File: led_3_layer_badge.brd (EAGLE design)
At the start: 160 x 100 mm, 59 parts, among them U1 ATMEGA168, U2 MCP73811, U3 AP34063, U4 PCA9952

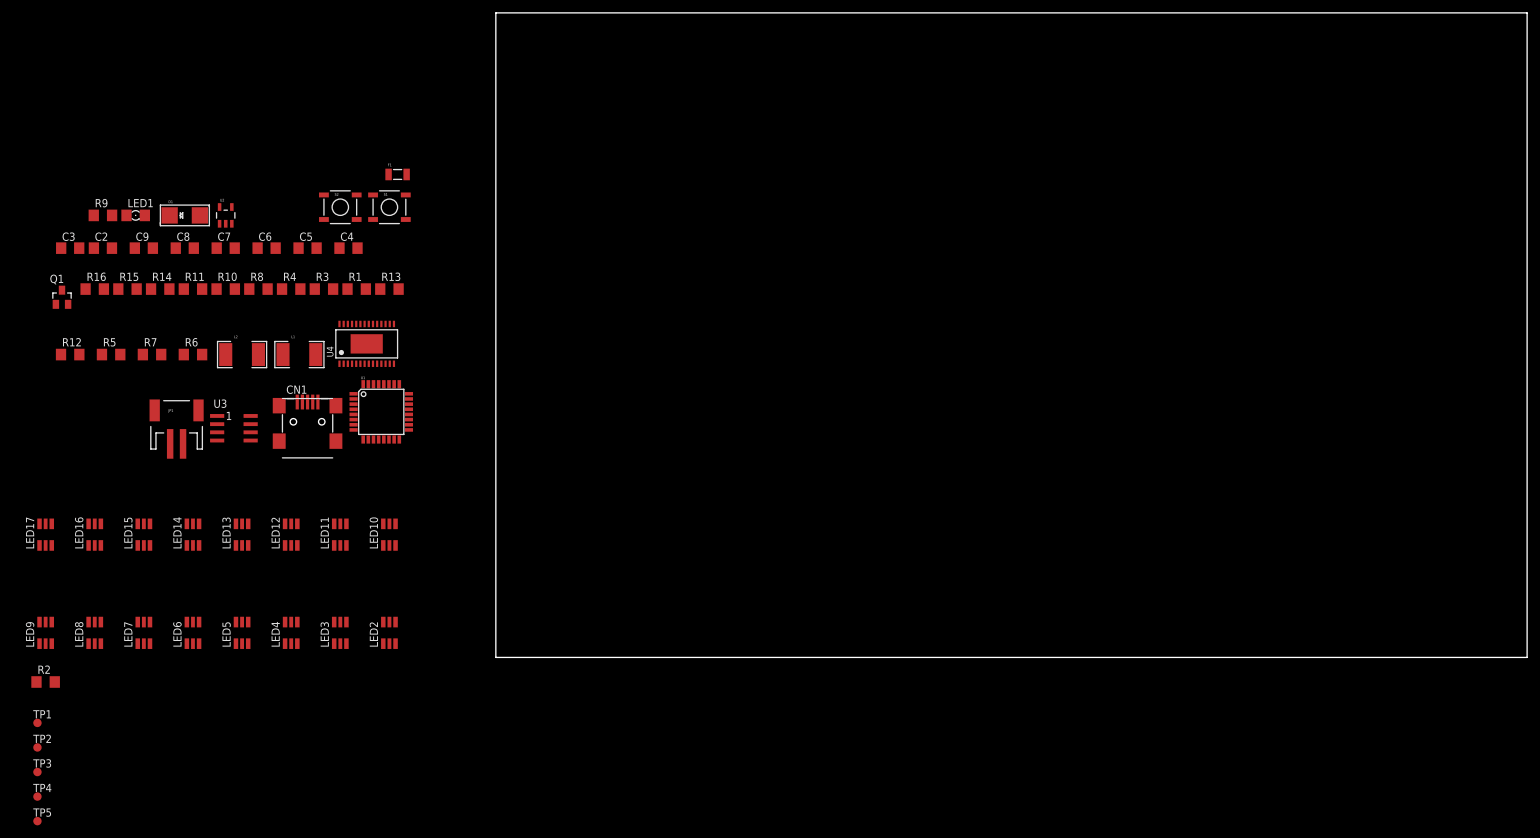
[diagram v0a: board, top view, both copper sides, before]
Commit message: added new concept image, found proper leds
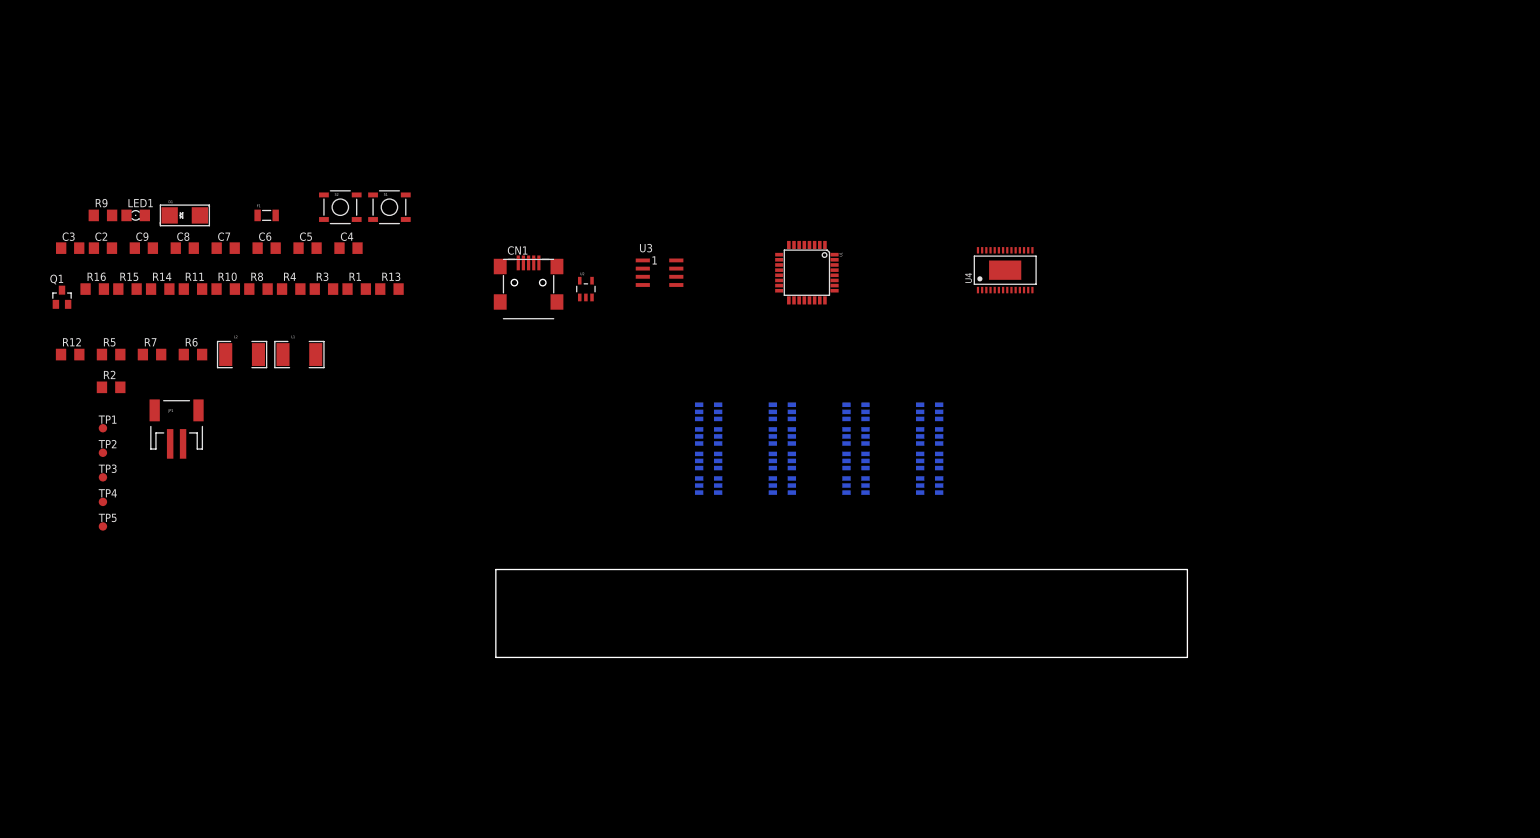
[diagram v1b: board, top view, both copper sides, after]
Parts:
- LED10, LED11, LED12, LED13, LED14, LED15, LED16, LED17, LED2, LED3, LED4, LED5, LED6, LED7, LED8, LED9: value GM5WA94310A -> GFTG-T7AW; device led:GM5WA94310A -> osram:C63062-A4-7-A1-01
- moved LED6 117.4 mm to (67.3, 30.5), flipped to the bottom, turned to 180 degrees
- moved LED14 115.9 mm to (67.3, 38.1), flipped to the bottom, turned to 180 degrees
- moved LED7 113.7 mm to (55.9, 30.5), flipped to the bottom, turned to 180 degrees
- moved LED15 112.1 mm to (55.9, 38.1), flipped to the bottom, turned to 180 degrees
- moved LED8 110.0 mm to (44.5, 30.5), flipped to the bottom, turned to 180 degrees
- moved LED16 108.4 mm to (44.5, 38.1), flipped to the bottom, turned to 180 degrees
- moved LED9 106.3 mm to (33.0, 30.5), flipped to the bottom, turned to 180 degrees
- moved LED17 104.6 mm to (33.0, 38.1), flipped to the bottom, turned to 180 degrees
- moved U4 99.7 mm to (78.7, 59.7)
- moved LED2 86.9 mm to (67.3, 26.7), flipped to the bottom, turned to 180 degrees
- moved LED10 85.2 mm to (67.3, 34.3), flipped to the bottom, turned to 180 degrees
- moved LED3 83.2 mm to (55.9, 26.7), flipped to the bottom, turned to 180 degrees
- moved LED11 81.4 mm to (55.9, 34.3), flipped to the bottom, turned to 180 degrees
- moved LED4 79.6 mm to (44.5, 26.7), flipped to the bottom, turned to 180 degrees
- moved LED12 77.7 mm to (44.5, 34.3), flipped to the bottom, turned to 180 degrees
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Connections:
- net A0: now also LED2.C3; no longer LED2.5
- net A1: now also LED2.C2; no longer LED2.4
- net A2: now also LED2.C1; no longer LED2.6
- net B0: now also LED10.C3; no longer LED10.5
- net B1: now also LED10.C2; no longer LED10.4
- net B2: now also LED10.C1; no longer LED10.6
- net C0: now also LED6.C3; no longer LED6.5
- net C1: now also LED6.C2; no longer LED6.4
- net C2: now also LED6.C1; no longer LED6.6
- net D0: now also LED14.C3; no longer LED14.5
- net D1: now also LED14.C2; no longer LED14.4
- net D2: now also LED14.C1; no longer LED14.6
- net N$10: now also LED17.A1, LED17.A2, LED17.A3; no longer LED17.1, LED17.2, LED17.3
- net N$12: now also LED6.A1, LED7.C1; no longer LED6.2, LED7.5
- net N$16: now also LED6.A2, LED7.C2; no longer LED6.3, LED7.4
- net N$17: now also LED6.A3, LED7.C3; no longer LED6.1, LED7.6
- net N$18: now also LED7.A1, LED8.C1; no longer LED8.2, LED9.5
- net N$19: now also LED7.A2, LED8.C2; no longer LED8.3, LED9.4
- net N$2: now also LED2.A1, LED3.C1; no longer LED2.2, LED3.5
- net N$20: now also LED7.A3, LED8.C3; no longer LED8.1, LED9.6
- net N$21: now also LED8.A1, LED9.C1; no longer LED7.2, LED8.5
- net N$22: now also LED8.A2, LED9.C2; no longer LED7.3, LED8.4
- net N$24: now also LED2.A2, LED3.C2; no longer LED2.3, LED3.4
- net N$25: now also LED2.A3, LED3.C3; no longer LED2.1, LED3.6
- net N$28: now also LED3.A1, LED4.C1; no longer LED4.2, LED5.5
- net N$29: now also LED3.A2, LED4.C2; no longer LED4.3, LED5.4
- net N$30: now also LED3.A3, LED4.C3; no longer LED4.1, LED5.6
- net N$31: now also LED4.A1, LED5.C1; no longer LED3.2, LED4.5
- net N$32: now also LED4.A2, LED5.C2; no longer LED3.3, LED4.4
- net N$33: now also LED4.A3, LED5.C3; no longer LED3.1, LED4.6
- net N$34: now also LED8.A3, LED9.C3; no longer LED7.1, LED8.6
- net N$35: now also LED10.A1, LED11.C1; no longer LED10.2, LED11.5
- net N$36: now also LED10.A2, LED11.C2; no longer LED10.3, LED11.4
- net N$37: now also LED10.A3, LED11.C3; no longer LED10.1, LED11.6
- net N$38: now also LED11.A1, LED12.C1; no longer LED12.2, LED13.5
- net N$39: now also LED11.A2, LED12.C2; no longer LED12.3, LED13.4
- net N$40: now also LED11.A3, LED12.C3; no longer LED12.1, LED13.6
- net N$41: now also LED12.A1, LED13.C1; no longer LED11.2, LED12.5
- net N$42: now also LED12.A2, LED13.C2; no longer LED11.3, LED12.4
- net N$43: now also LED12.A3, LED13.C3; no longer LED11.1, LED12.6
- net N$44: now also LED14.A1, LED15.C1; no longer LED14.2, LED15.5
- net N$45: now also LED14.A2, LED15.C2; no longer LED14.3, LED15.4
- net N$46: now also LED14.A3, LED15.C3; no longer LED14.1, LED15.6
- net N$47: now also LED15.A1, LED16.C1; no longer LED16.2, LED17.5
- net N$48: now also LED15.A2, LED16.C2; no longer LED16.3, LED17.4
- net N$49: now also LED15.A3, LED16.C3; no longer LED16.1, LED17.6
- net N$50: now also LED16.A1, LED17.C1; no longer LED15.2, LED16.5
- net N$51: now also LED16.A2, LED17.C2; no longer LED15.3, LED16.4
- net N$52: now also LED16.A3, LED17.C3; no longer LED15.1, LED16.6
- net VCC/2: now also LED13.A1, LED13.A2, LED13.A3, LED5.A1, LED5.A2, LED5.A3, LED9.A1, LED9.A2, LED9.A3; no longer LED13.1, LED13.2, LED13.3, LED5.1, LED5.2, LED5.3, LED9.1, LED9.2, LED9.3
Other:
- board size 160 x 100 mm -> 107.3 x 13.6 mm

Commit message: revisions
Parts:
- removed JP1: (no value), sparkfun:JST-2-SMD
- removed R11: 10k, rcl:R1206
- removed U1: ATMEGA168, sparkfun:TQFP32-08
- added IC1: TINY24/44/84, atmel:SOIC14
- added TP6, TP7: PTR1B2,54, testpad:B2,54
- Q1: value (none) -> P-CH
- U3: value AP34063 -> MC33063A
- moved R8 76.9 mm to (-66.0, -14.0)
- moved U4 55.1 mm to (92.7, 6.35)
- moved U3 54.6 mm to (24.1, 5.08)
- moved CN1 54.1 mm to (14.0, 3.81)
- moved U2 46.4 mm to (21.6, 11.4), turned to 270 degrees
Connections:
- removed net !SHDN: Q1.1, R8.1, U1.9
- removed net N$53: TP1.TP, U1.17
- removed net N$54: TP2.TP, U1.16
- removed net N$55: TP3.TP, U1.15
- removed net RX: U1.30
- removed net TX: U1.31
- new net MOSI: IC1.8, TP1.TP
- net !OE: now also IC1.12, Q1.1, R8.2; no longer R11.2, U1.2
- net !RST: now also IC1.4; no longer U1.29
- net GND: now also IC1.14, TP7.TP; no longer JP1.2, R8.2, U1.21, U1.3, U1.5
- net N$7: now also Q1.3; no longer Q1.2
- net S1: now also IC1.10; no longer U1.32
- net S2: now also IC1.11; no longer U1.1
- net SCL: now also IC1.9, TP2.TP; no longer U1.28
- net SDA: now also IC1.7, TP3.TP; no longer U1.27
- net VCC: now also IC1.1, IC1.13, Q1.2, R8.1, TP6.TP; no longer JP1.1, Q1.3, R11.1, U1.18, U1.20, U1.4, U1.6
